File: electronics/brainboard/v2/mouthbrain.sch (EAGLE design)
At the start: 28 parts, among them Q1 MOSFET-NCHANNELSMD, Q10 MOSFET-NCHANNELSMD, Q11 MOSFET-NCHANNELSMD, Q12 MOSFET-NCHANNELSMD, Q13 MOSFET-NCHANNELSMD, Q14 MOSFET-NCHANNELSMD, Q15 MOSFET-NCHANNELSMD, Q16 MOSFET-NCHANNELSMD, Q2 MOSFET-NCHANNELSMD, Q3 MOSFET-NCHANNELSMD, Q4 MOSFET-NCHANNELSMD, Q5 MOSFET-NCHANNELSMD, Q6 MOSFET-NCHANNELSMD, Q7 MOSFET-NCHANNELSMD, Q8 MOSFET-NCHANNELSMD, Q9 MOSFET-NCHANNELSMD, U2 ARDUINO-MEGAFULL

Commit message: circuit is ready to rock and roll.
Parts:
- removed JP2: (no value), SparkFun:M023.5MM
- removed U$3, U$4, U$5, U$6: MCP4352, mouthbrain:MCP4352
- added MEGA: ARDUINO-MEGAFULL, SparkFun:ARDUINO-MEGAFULL
- added U$2: FPC-0.5-32, Hoektronics:FPC-0.5-32
- added U1, U3, U4: MCP4352, mouthbrain:MCP4352
- added U5: MOSFET-NCHANNEL-SOIC8, SparkFun:MOSFET-NCHANNEL-SOIC8
- U$1: value MOSFET-NCHANNEL-SOIC8 -> DC-DC-CONVERTER; device SparkFun:MOSFET-NCHANNEL-SOIC8 -> Hoektronics:DC-DC-CONVERTER
- U2: value ARDUINO-MEGAFULL -> MCP4352; device SparkFun:ARDUINO-MEGAFULL -> mouthbrain:MCP4352
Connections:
- removed net AN0: Q1.G, U2.22
- removed net AN1: Q2.G, U2.23
- removed net AN10: Q11.G, U2.32
- removed net AN11: Q12.G, U2.33
- removed net AN12: Q13.G, U2.34
- removed net AN13: Q14.G, U2.35
- removed net AN14: Q15.G, U2.36
- removed net AN15: Q16.G
- removed net AN2: Q3.G, U2.24
- removed net AN3: Q4.G, U2.25
- removed net AN4: Q5.G, U2.26
- removed net AN5: Q6.G, U2.27
- removed net AN6: Q7.G, U2.28
- removed net AN7: Q8.G, U2.29
- removed net AN8: Q9.G, U2.30
- removed net AN9: Q10.G, U2.31
- removed net ANODE0: Q1.D
- removed net ANODE1: Q2.D
- removed net ANODE10: Q11.D
- removed net ANODE11: Q12.D
- removed net ANODE12: Q13.D
- removed net ANODE13: Q14.D
- removed net ANODE14: Q15.D
- removed net ANODE15: Q16.D
- removed net ANODE2: Q3.D
- removed net ANODE3: Q4.D
- removed net ANODE4: Q5.D
- removed net ANODE5: Q6.D
- removed net ANODE6: Q7.D
- removed net ANODE7: Q8.D
- removed net ANODE8: Q9.D
- removed net ANODE9: Q10.D
- removed net N$3: C1.1, D1.C
- removed net OUT0: U$3.P0W, U2.A0(RX0)
- removed net OUT1: U$3.P1W, U2.A1(TX0)
- removed net OUT10: U$5.P2W, U2.A10
- removed net OUT11: U$5.P3W, U2.A11
- removed net OUT12: U$6.P0W, U2.A12
- removed net OUT13: U$6.P1W, U2.A13
- removed net OUT14: U$6.P2W, U2.A14
- removed net OUT15: U$6.P3W, U2.A15
- removed net OUT2: U$3.P2W, U2.A2
- removed net OUT3: U$3.P3W, U2.A3
- removed net OUT4: U$4.P0W, U2.A4
- removed net OUT5: U$4.P1W, U2.A5
- removed net OUT6: U$4.P2W, U2.A6
- removed net OUT7: U$4.P3W, U2.A7
- removed net OUT8: U$5.P0W, U2.A8
- removed net OUT9: U$5.P1W, U2.A9
- new net AOUT0: MEGA.A0(RX0), U$2.2, U1.P0W
- new net AOUT1: MEGA.A1(TX0), U$2.4, U1.P1W
- new net AOUT10: MEGA.A10, U$2.22, U3.P2W
- new net AOUT11: MEGA.A11, U$2.24, U3.P3W
- new net AOUT12: MEGA.A12, U$2.26, U4.P0W
- new net AOUT13: MEGA.A13, U$2.28, U4.P1W
- new net AOUT14: MEGA.A14, U$2.30, U4.P2W
- new net AOUT15: MEGA.A15, U$2.32, U4.P3W
- new net AOUT2: MEGA.A2, U$2.6, U1.P2W
- new net AOUT3: MEGA.A3, U$2.8, U1.P3W
- new net AOUT4: MEGA.A4, U$2.10, U2.P0W
- new net AOUT5: MEGA.A5, U$2.12, U2.P1W
- new net AOUT6: MEGA.A6, U$2.14, U2.P2W
- new net AOUT7: MEGA.A7, U$2.16, U2.P3W
- new net AOUT8: MEGA.A8, U$2.18, U3.P0W
- new net AOUT9: MEGA.A9, U3.P1W
- new net CIN0: MEGA.22, Q1.G
- new net CIN1: MEGA.23, Q2.G
- new net CIN10: MEGA.32, Q11.G
- new net CIN11: MEGA.33, Q12.G
- new net CIN12: MEGA.34, Q13.G
- new net CIN13: MEGA.35, Q14.G
- new net CIN14: MEGA.36, Q15.G
- new net CIN15: MEGA.37, Q16.G
- new net CIN2: MEGA.24, Q3.G
- new net CIN3: MEGA.25, Q4.G
- new net CIN4: MEGA.26, Q5.G
- new net CIN5: MEGA.27, Q6.G
- new net CIN6: MEGA.28, Q7.G
- new net CIN7: MEGA.29, Q8.G
- new net CIN8: MEGA.30, Q9.G
- new net CIN9: MEGA.31, Q10.G
- new net COUT0: Q1.D, U$2.1
- new net COUT1: Q2.D, U$2.3
- new net COUT10: Q11.D, U$2.21
- new net COUT11: Q12.D, U$2.23
- new net COUT12: Q13.D, U$2.25
- new net COUT13: Q14.D, U$2.27
- new net COUT14: Q15.D, U$2.29
- new net COUT15: Q16.D, U$2.31
- new net COUT2: Q3.D, U$2.5
- new net COUT3: Q4.D, U$2.7
- new net COUT4: Q5.D, U$2.9
- new net COUT5: Q6.D, U$2.11
- new net COUT6: Q7.D, U$2.13
- new net COUT7: Q8.D, U$2.15
- new net COUT8: Q9.D, U$2.17
- new net COUT9: Q10.D, U$2.19, U$2.20
- net !CS1: now also MEGA.6, U1.!CS; no longer U$3.!CS, U2.6
- net !CS2: now also MEGA.7, U2.!CS; no longer U$4.!CS, U2.7
- net !CS3: now also MEGA.8, U3.!CS; no longer U$5.!CS, U2.8
- net !CS4: now also MEGA.9, U4.!CS; no longer U$6.!CS, U2.9
- net !RESET: now also MEGA.2, U1.!RESET, U2.!RESET, U3.!RESET, U4.!RESET; no longer U$3.!RESET, U$4.!RESET, U$5.!RESET, U$6.!RESET, U2.2
- net BOOST: now also C1.1, D1.C
- net BOOST_FET: now also MEGA.11, U5.G; no longer U$1.G
- net EXT: now also U$1.OUT+; no longer JP2.1
- net GND: now also MEGA.GND@0, MEGA.GND@1, MEGA.GND@2, MEGA.GND@3, MEGA.GND@4, U$1.IN-, U$1.OUT-, U1.GND, U1.P0B, U1.P1B, U1.P2B, U1.P3B, U2.GND, U2.P0B, U2.P1B, U2.P2B, U2.P3B, U3.GND, U3.P0B, U3.P1B, U3.P2B, U3.P3B, U4.GND, U4.P0B, U4.P1B, U4.P2B, U4.P3B, U5.D@1, U5.D@2, U5.D@3, U5.D@4; no longer JP2.2, U$1.D@1, U$1.D@2, U$1.D@3, U$1.D@4, U$3.GND, U$4.GND, U$5.GND, U$6.GND, U2.GND@0, U2.GND@1, U2.GND@2, U2.GND@3, U2.GND@4
- net N$1: now also U5.S@1, U5.S@2, U5.S@3; no longer U$1.S@1, U$1.S@2, U$1.S@3
- net SCK: now also MEGA.3, U1.SCK, U2.SCK, U3.SCK, U4.SCK; no longer U$3.SCK, U$4.SCK, U$5.SCK, U$6.SCK, U2.3
- net SI: now also MEGA.4, U1.SI, U2.SI, U3.SI, U4.SI; no longer U$3.SI, U$4.SI, U$5.SI, U$6.SI, U2.4
- net SO: now also MEGA.5; no longer U2.5
- net VCC: now also U$1.IN+, U1.VCC, U2.VCC, U3.VCC, U4.VCC; no longer U$3.VCC, U$4.VCC, U$5.VCC, U$6.VCC
- net VDD: now also U1.P0A, U1.P1A, U1.P2A, U1.P3A, U2.P0A, U2.P1A, U2.P2A, U2.P3A, U3.P0A, U3.P1A, U3.P2A, U3.P3A, U4.P0A, U4.P1A, U4.P2A, U4.P3A; no longer U$3.P0A, U$3.P1A, U$3.P2A, U$3.P3A, U$4.P0A, U$4.P1A, U$4.P2A, U$4.P3A, U$5.P0A, U$5.P1A, U$5.P2A, U$5.P3A, U$6.P0A, U$6.P1A, U$6.P2A, U$6.P3A
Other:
- moved on the sheet: C1, C2, D1, L1, Q1, Q10, Q11, Q12, Q13, Q14, Q15, Q16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

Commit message: routed a bunch of the brainboard.
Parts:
- removed MEGA: ARDUINO-MEGAFULL, SparkFun:ARDUINO-MEGAFULL
- added U$3: ARDUINO-MEGA, Hoektronics:ARDUINO-MEGA
- U$2: value FPC-0.5-32 -> FPC-0.5-32HORIZ; device Hoektronics:FPC-0.5-32 -> Hoektronics:FPC-0.5-32HORIZ
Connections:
- net !CS1: now also U$3.D6; no longer MEGA.6
- net !CS2: now also U$3.D5; no longer MEGA.7
- net !CS3: now also U$3.D4; no longer MEGA.8
- net !CS4: now also U$3.D3; no longer MEGA.9
- net !RESET: now also U$3.D2; no longer MEGA.2
- net AOUT0: now also U$3.A0, U1.P1W; no longer MEGA.A0(RX0), U1.P0W
- net AOUT1: now also U$3.A1, U1.P0W; no longer MEGA.A1(TX0), U1.P1W
- net AOUT10: now also U$3.A10; no longer MEGA.A10
- net AOUT11: now also U$3.A11; no longer MEGA.A11
- net AOUT12: now also U$3.A12, U4.P1W; no longer MEGA.A12, U4.P0W
- net AOUT13: now also U$3.A13, U4.P0W; no longer MEGA.A13, U4.P1W
- net AOUT14: now also U$3.A14; no longer MEGA.A14
- net AOUT15: now also U$3.A15; no longer MEGA.A15
- net AOUT2: now also U$3.A2; no longer MEGA.A2
- net AOUT3: now also U$3.A3; no longer MEGA.A3
- net AOUT4: now also U$3.A4, U2.P1W; no longer MEGA.A4, U2.P0W
- net AOUT5: now also U$3.A5, U2.P0W; no longer MEGA.A5, U2.P1W
- net AOUT6: now also U$3.A6; no longer MEGA.A6
- net AOUT7: now also U$3.A7; no longer MEGA.A7
- net AOUT8: now also U$3.A8, U3.P1W; no longer MEGA.A8, U3.P0W
- net AOUT9: now also U$2.20, U$3.A9, U3.P0W; no longer MEGA.A9, U3.P1W
- net BOOST_FET: now also U$3.D11; no longer MEGA.11
- net CIN0: now also U$3.D22; no longer MEGA.22
- net CIN1: now also U$3.D24; no longer MEGA.23
- net CIN10: now also U$3.D42; no longer MEGA.32
- net CIN11: now also U$3.D44; no longer MEGA.33
- net CIN12: now also U$3.D46; no longer MEGA.34
- net CIN13: now also U$3.D48; no longer MEGA.35
- net CIN14: now also U$3.D50; no longer MEGA.36
- net CIN15: now also U$3.D52; no longer MEGA.37
- net CIN2: now also U$3.D26; no longer MEGA.24
- net CIN3: now also U$3.D28; no longer MEGA.25
- net CIN4: now also U$3.D30; no longer MEGA.26
- net CIN5: now also U$3.D32; no longer MEGA.27
- net CIN6: now also U$3.D34; no longer MEGA.28
- net CIN7: now also U$3.D36; no longer MEGA.29
- net CIN8: now also U$3.D38; no longer MEGA.30
- net CIN9: now also U$3.D40; no longer MEGA.31
- net COUT9: no longer U$2.20
- net GND: now also U$3.GND4, U$3.GND5; no longer MEGA.GND@0, MEGA.GND@1, MEGA.GND@2, MEGA.GND@3, MEGA.GND@4
- net SCK: now also U$3.D7; no longer MEGA.3
- net SI: now also U$3.D8; no longer MEGA.4
- net SO: now also U$3.D9; no longer MEGA.5
- net VCC: now also U$3.5V2

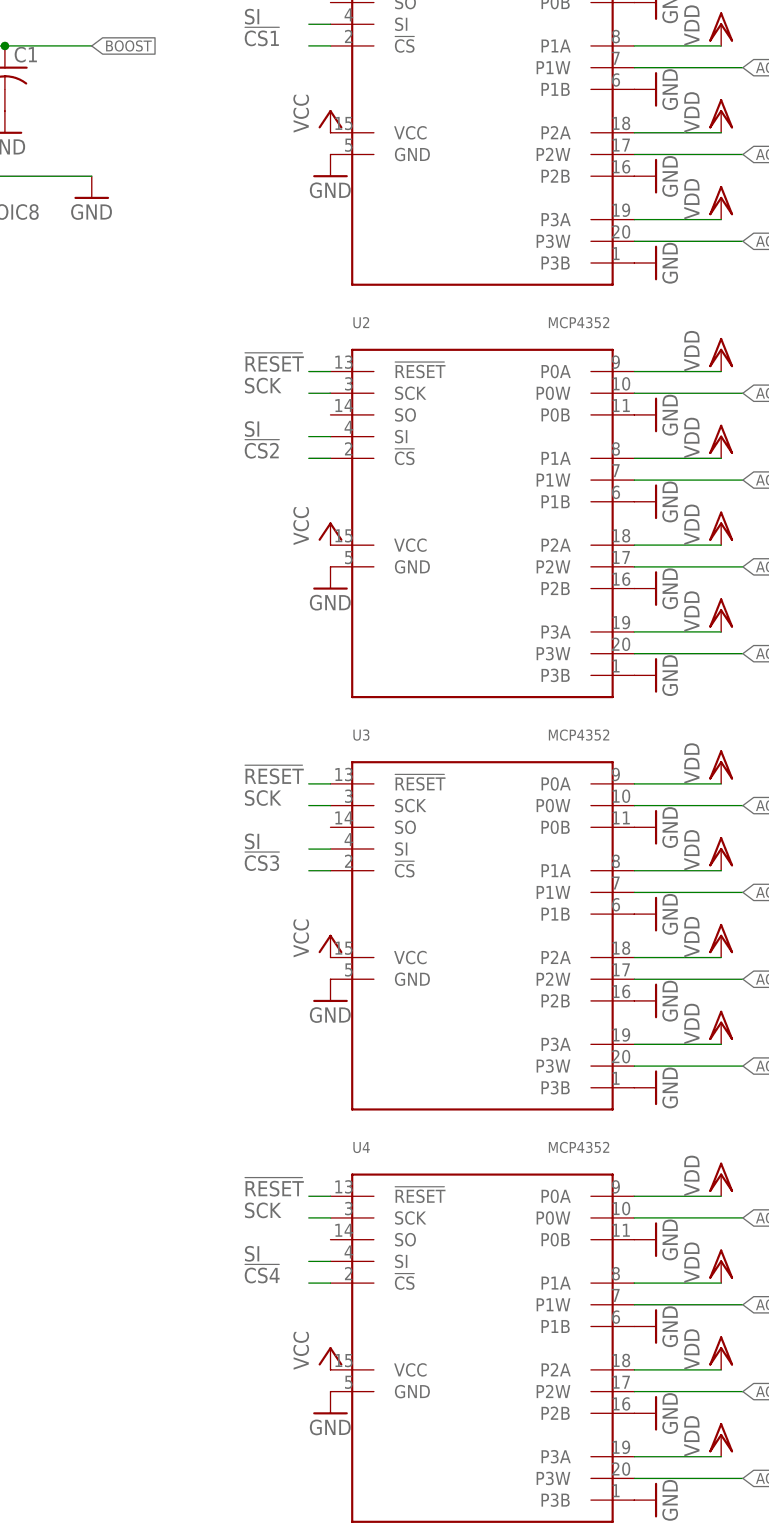
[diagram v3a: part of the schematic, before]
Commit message: switched ADCs to package with ground pad
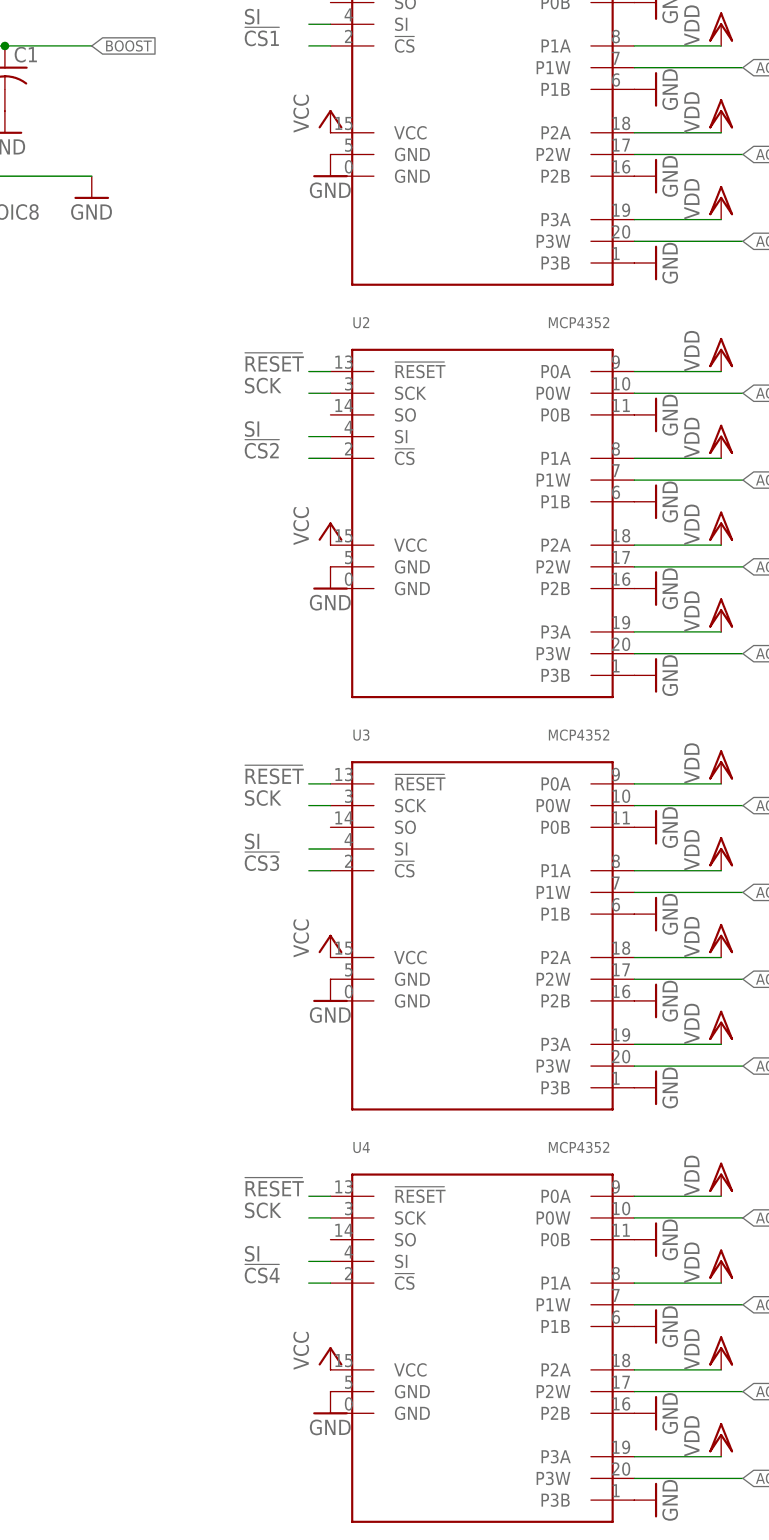
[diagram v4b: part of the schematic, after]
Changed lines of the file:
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@@
 <?xml version="1.0" encoding="utf-8"?>
 <!DOCTYPE eagle SYSTEM "eagle.dtd">
-<eagle version="6.4">
+<eagle version="6.4.1">
 <drawing>
 <settings>

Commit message: mouthbrain ready for prototyping.
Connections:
- net GND: now also U1.GND@2, U2.GND@2, U3.GND@2, U4.GND@2
